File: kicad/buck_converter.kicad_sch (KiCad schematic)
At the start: 46 parts, among them J5 SolderPad, J6 SolderPad, Q2 CSD19537Q3, Q3 BSZ096N10LS5, U2 LM5146

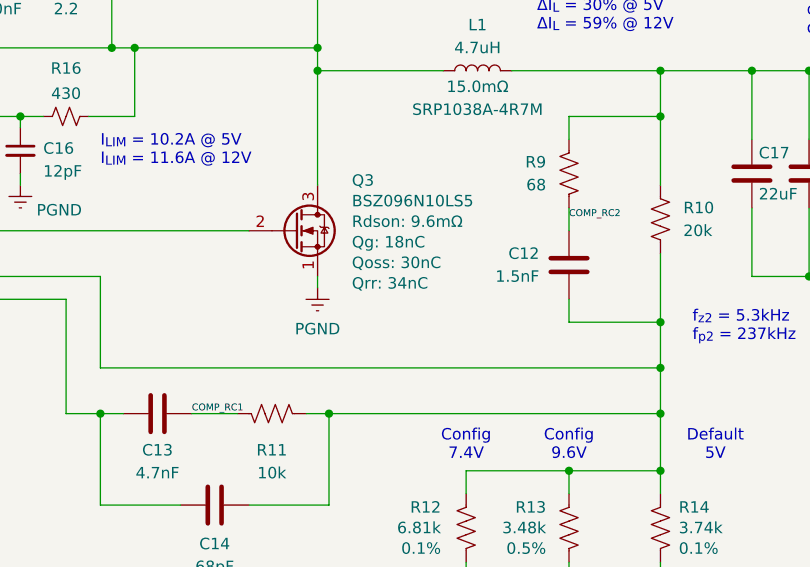
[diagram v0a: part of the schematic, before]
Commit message: Addressed HS FET failure mode from revC
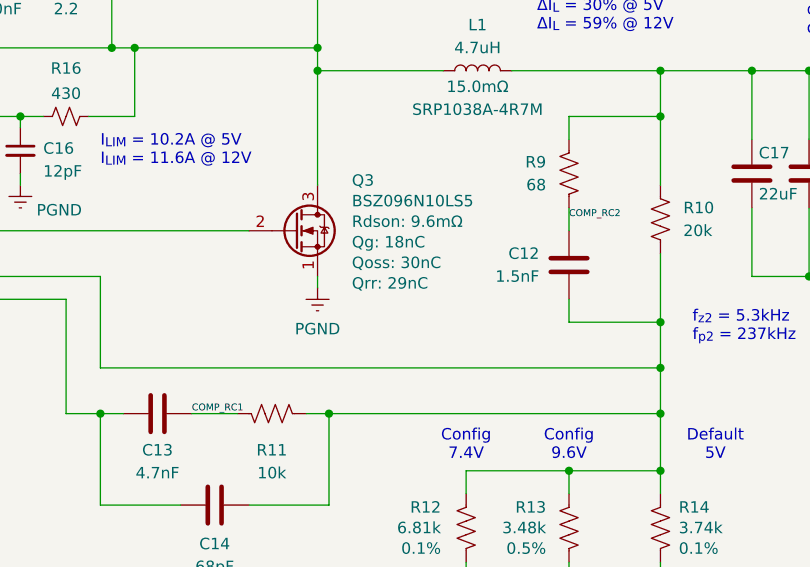
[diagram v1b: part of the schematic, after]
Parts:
- Q3: Qrr 34nC -> 29nC
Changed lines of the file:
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@@
 			)
 		)
-		(property "Qrr" "34nC"
+		(property "Qrr" "29nC"
 			(at 157.48 97.282 0)
 			(show_name yes)
